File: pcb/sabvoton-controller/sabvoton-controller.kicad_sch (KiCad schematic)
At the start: 27 parts, among them J1 Conn_02x03_Counter_Clockwise, J2 Conn_01x30, U1 ESP32-WROOM-32, U2 XL7015E1, U3 XL7015E1

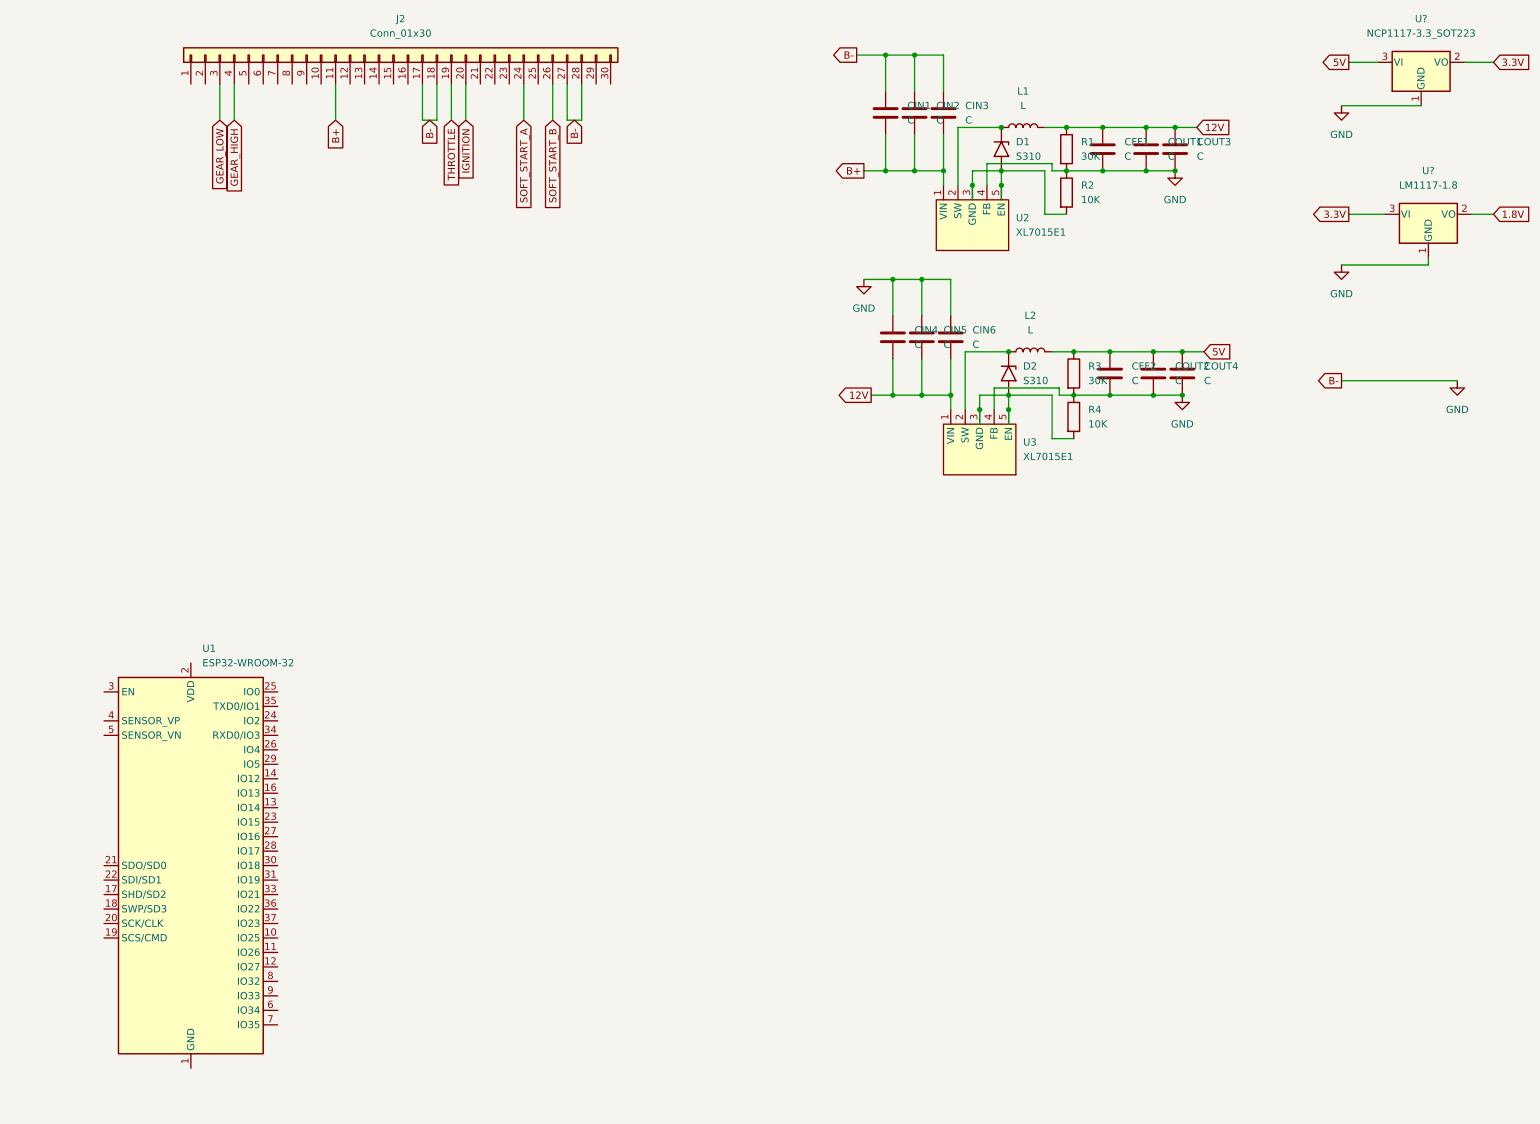
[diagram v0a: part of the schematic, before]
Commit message: Added power to the ESP32
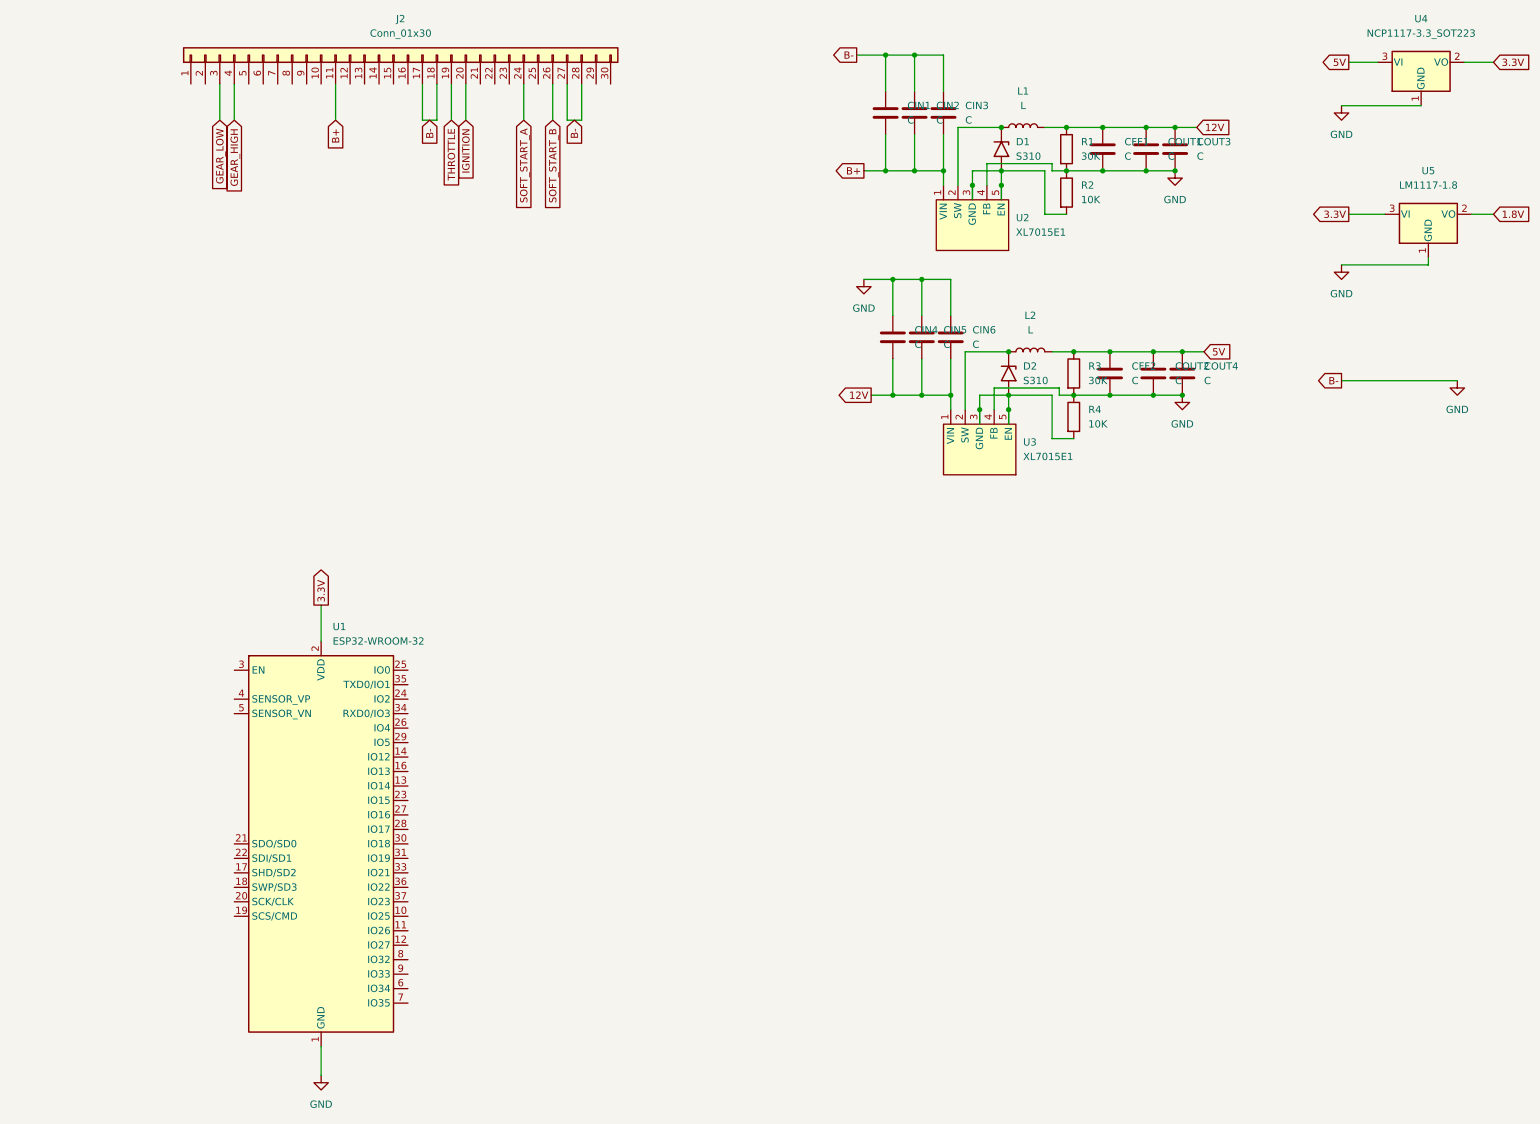
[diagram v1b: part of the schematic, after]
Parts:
- gave numbers to parts that had none: 2
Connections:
- net 3.3V: now also U1.2 (VDD)
- net GND: now also U1.1 (GND), U1.15 (GND), U1.38 (GND), U1.39 (GND)
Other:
- moved on the sheet: U1
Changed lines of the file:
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@@
+    (stroke (width 0) (type default) (color 0 0 0 0))
+  )
+  (wire (pts (xy 392.43 228.6) (xy 392.43 233.68))
     (stroke (width 0) (type default) (color 0 0 0 0))
   )
@@
     (stroke (width 0) (type default) (color 0 0 0 0))
   )
+  (wire (pts (xy 392.43 151.13) (xy 392.43 157.48))
+    (stroke (width 0) (type default) (color 0 0 0 0))
+  )
   (wire (pts (xy 571.5 63.5) (xy 585.47 63.5))
     (stroke (width 0) (type default) (color 0 0 0 0))
@@
   (wire (pts (xy 435.61 59.69) (xy 435.61 66.04))
     (stroke (width 0) (type default) (color 0 0 0 0))
+  )
+  (global_label "3.3V" (shape output) (at 392.43 151.13 90) (fields_autoplaced)
+    (effects (font (size 1.27 1.27)) (justify left))
+    (property "Intersheet References" "${INTERSHEET_REFS}" (id 0) (at 392.5094 144.6045 90)
+      (effects (font (size 1.27 1.27)) (justify left) hide)
+    )
   )
   (global_label "5V" (shape input) (at 547.37 106.68 0) (fields_autoplaced)
@@
   (symbol (lib_id "Regulator_Linear:LM1117-1.8") (at 586.74 82.55 0) (unit 1)
     (in_bom yes) (on_board yes) (fields_autoplaced)
-    (property "Reference" "U?" (id 0) (at 586.74 74.93 0))
+    (property "Reference" "U5" (id 0) (at 586.74 74.93 0))
     (property "Value" "LM1117-1.8" (id 1) (at 586.74 77.47 0))
     (property "Footprint" "Package_TO_SOT_SMD:SOT-223-3_TabPin2" (id 2) (at 586.74 82.55 0)
@@
     (pin "2")
   )
+  (symbol (lib_id "power:GND") (at 392.43 233.68 0) (unit 1)
+    (in_bom yes) (on_board yes) (fields_autoplaced)
+    (property "Reference" "#PWR0101" (id 0) (at 392.43 240.03 0)
+      (effects (font (size 1.27 1.27)) hide)
+    )
+    (property "Value" "GND" (id 1) (at 392.43 238.76 0))
+    (property "Footprint" "" (id 2) (at 392.43 233.68 0)
+      (effects (font (size 1.27 1.27)) hide)
+    )
+    (property "Datasheet" "" (id 3) (at 392.43 233.68 0)
+      (effects (font (size 1.27 1.27)) hide)
+    )
+    (pin "1")
+  )
   (symbol (lib_id "Diode:1.5KExxA") (at 511.81 71.12 270) (unit 1)
     (in_bom yes) (on_board yes) (fields_autoplaced)
@@
   (symbol (lib_id "power:GND") (at 571.5 63.5 0) (unit 1)
     (in_bom yes) (on_board yes) (fields_autoplaced)
-    (property "Reference" "#PWR?" (id 0) (at 571.5 69.85 0)
+    (property "Reference" "#PWR0102" (id 0) (at 571.5 69.85 0)
       (effects (font (size 1.27 1.27)) hide)
     )
@@
   (symbol (lib_id "power:GND") (at 591.82 111.76 0) (unit 1)
     (in_bom yes) (on_board yes) (fields_autoplaced)
-    (property "Reference" "#PWR?" (id 0) (at 591.82 118.11 0)
+    (property "Reference" "#PWR0103" (id 0) (at 591.82 118.11 0)
       (effects (font (size 1.27 1.27)) hide)
     )
@@
   (symbol (lib_id "Regulator_Linear:NCP1117-3.3_SOT223") (at 585.47 55.88 0) (unit 1)
     (in_bom yes) (on_board yes) (fields_autoplaced)
-    (property "Reference" "U?" (id 0) (at 585.47 48.26 0))
+    (property "Reference" "U4" (id 0) (at 585.47 48.26 0))
     (property "Value" "NCP1117-3.3_SOT223" (id 1) (at 585.47 50.8 0))
     (property "Footprint" "Package_TO_SOT_SMD:SOT-223-3_TabPin2" (id 2) (at 585.47 50.8 0)
@@
     (pin "2")
   )
-  (symbol (lib_id "RF_Module:ESP32-WROOM-32") (at 369.57 196.85 0) (unit 1)
-    (in_bom yes) (on_board yes) (fields_autoplaced)
-    (property "Reference" "U1" (id 0) (at 371.5894 158.75 0)
-      (effects (font (size 1.27 1.27)) (justify left))
-    )
-    (property "Value" "ESP32-WROOM-32" (id 1) (at 371.5894 161.29 0)
-      (effects (font (size 1.27 1.27)) (justify left))
-    )
-    (property "Footprint" "RF_Module:ESP32-WROOM-32" (id 2) (at 369.57 234.95 0)
-      (effects (font (size 1.27 1.27)) hide)
-    )
-    (property "Datasheet" "https://www.espressif.com/sites/default/files/documentation/esp32-wroom-32_datasheet_en.pdf" (id 3) (at 361.95 195.58 0)
+  (symbol (lib_id "RF_Module:ESP32-WROOM-32") (at 392.43 193.04 0) (unit 1)
+    (in_bom yes) (on_board yes) (fields_autoplaced)
+    (property "Reference" "U1" (id 0) (at 394.4494 154.94 0)
+      (effects (font (size 1.27 1.27)) (justify left))
+    )
+    (property "Value" "ESP32-WROOM-32" (id 1) (at 394.4494 157.48 0)
+      (effects (font (size 1.27 1.27)) (justify left))
+    )
+    (property "Footprint" "RF_Module:ESP32-WROOM-32" (id 2) (at 392.43 231.14 0)
+      (effects (font (size 1.27 1.27)) hide)
+    )
+    (property "Datasheet" "https://www.espressif.com/sites/default/files/documentation/esp32-wroom-32_datasheet_en.pdf" (id 3) (at 384.81 191.77 0)
       (effects (font (size 1.27 1.27)) hide)
     )
@@
   (symbol (lib_id "power:GND") (at 571.5 91.44 0) (unit 1)
     (in_bom yes) (on_board yes) (fields_autoplaced)
-    (property "Reference" "#PWR?" (id 0) (at 571.5 97.79 0)
+    (property "Reference" "#PWR0104" (id 0) (at 571.5 97.79 0)
       (effects (font (size 1.27 1.27)) hide)
     )
@@
       (reference "#PWR03") (unit 1) (value "GND") (footprint "")
     )
+    (path "/503c752c-7842-4267-a639-6f3d9aa0fe2a"
+      (reference "#PWR0101") (unit 1) (value "GND") (footprint "")
+    )
     (path "/5282e63d-cfea-46aa-b976-c6a9cdec0d63"
-      (reference "#PWR?") (unit 1) (value "GND") (footprint "")
+      (reference "#PWR0102") (unit 1) (value "GND") (footprint "")
     )
     (path "/972aac5e-c9a1-4c35-9267-e07a8dc2778e"
-      (reference "#PWR?") (unit 1) (value "GND") (footprint "")
+      (reference "#PWR0103") (unit 1) (value "GND") (footprint "")
     )
     (path "/e7b8caad-8c25-46ee-a171-3c952ff2378f"
-      (reference "#PWR?") (unit 1) (value "GND") (footprint "")
+      (reference "#PWR0104") (unit 1) (value "GND") (footprint "")
     )
     (path "/d492c89a-b073-4f16-8a2d-e57b90ec8edc"
@@
       (reference "U3") (unit 1) (value "XL7015E1") (footprint "Package_TO_SOT_SMD:TO-252-5_TabPin3")
     )
+    (path "/9a47097d-06a5-4183-845e-85572096854c"
+      (reference "U4") (unit 1) (value "NCP1117-3.3_SOT223") (footprint "Package_TO_SOT_SMD:SOT-223-3_TabPin2")
+    )
     (path "/4029d2d4-cecc-41e8-82bd-e371ea31d069"
-      (reference "U?") (unit 1) (value "LM1117-1.8") (footprint "Package_TO_SOT_SMD:SOT-223-3_TabPin2")
-    )
-    (path "/9a47097d-06a5-4183-845e-85572096854c"
-      (reference "U?") (unit 1) (value "NCP1117-3.3_SOT223") (footprint "Package_TO_SOT_SMD:SOT-223-3_TabPin2")
-    )
-  )
+      (reference "U5") (unit 1) (value "LM1117-1.8") (footprint "Package_TO_SOT_SMD:SOT-223-3_TabPin2")
+    )
+  )

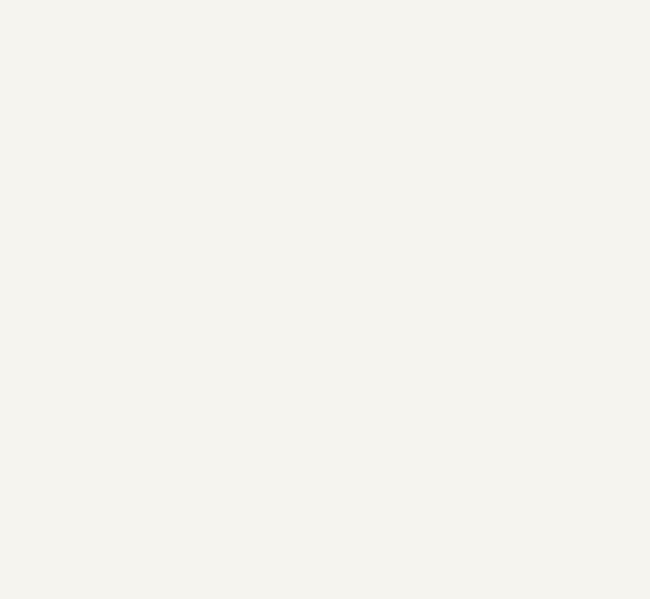
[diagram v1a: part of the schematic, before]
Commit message: Added power switch circuit
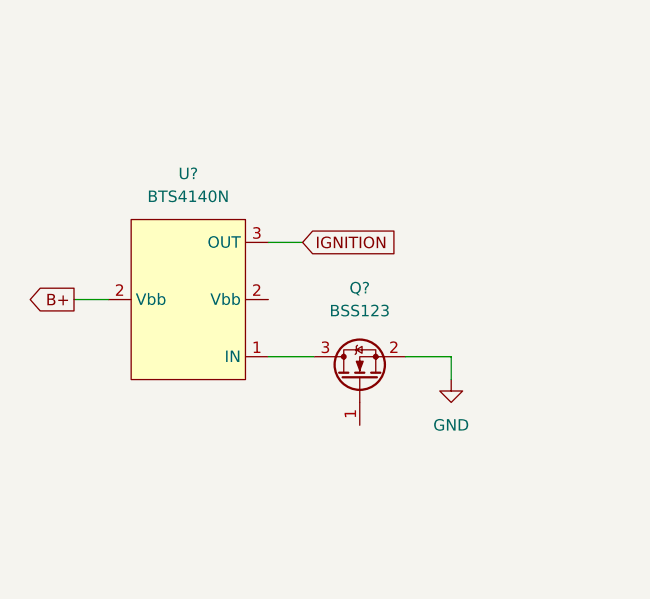
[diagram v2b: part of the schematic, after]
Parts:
- added Q?: BSS123, Package_TO_SOT_SMD:SOT-23, symbol Transistor_FET:BSS123
- added U?: BTS4140N, Package_TO_SOT_SMD:SOT-223-3_TabPin2, symbol KT_Display:BTS4140N
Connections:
- net B+: now also U?.2 (Vbb)
- net GND: now also Q?.2 (S)
- net IGNITION: now also U?.3 (OUT)
- new net: Q?.3 (D), U?.1 (IN)
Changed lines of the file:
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@@
+    (stroke (width 0) (type default) (color 0 0 0 0))
+  )
+  (wire (pts (xy 248.92 88.9) (xy 254 88.9))
     (stroke (width 0) (type default) (color 0 0 0 0))
   )
@@
     (stroke (width 0) (type default) (color 0 0 0 0))
   )
+  (wire (pts (xy 269.24 88.9) (xy 269.24 91.44))
+    (stroke (width 0) (type default) (color 0 0 0 0))
+  )
   (wire (pts (xy 427.99 59.69) (xy 427.99 66.04))
     (stroke (width 0) (type default) (color 0 0 0 0))
@@
     (stroke (width 0) (type default) (color 0 0 0 0))
   )
+  (wire (pts (xy 227.33 82.55) (xy 231.14 82.55))
+    (stroke (width 0) (type default) (color 0 0 0 0))
+  )
   (wire (pts (xy 487.68 74.93) (xy 491.49 74.93))
     (stroke (width 0) (type default) (color 0 0 0 0))
@@
     (stroke (width 0) (type default) (color 0 0 0 0))
   )
+  (wire (pts (xy 264.16 88.9) (xy 269.24 88.9))
+    (stroke (width 0) (type default) (color 0 0 0 0))
+  )
   (wire (pts (xy 496.57 54.61) (xy 496.57 60.96))
     (stroke (width 0) (type default) (color 0 0 0 0))
@@
   )
   (wire (pts (xy 496.57 68.58) (xy 496.57 74.93))
+    (stroke (width 0) (type default) (color 0 0 0 0))
+  )
+  (wire (pts (xy 248.92 76.2) (xy 252.73 76.2))
     (stroke (width 0) (type default) (color 0 0 0 0))
   )
@@
     )
   )
+  (global_label "B+" (shape output) (at 227.33 82.55 180) (fields_autoplaced)
+    (effects (font (size 1.27 1.27)) (justify right))
+    (property "Intersheet References" "${INTERSHEET_REFS}" (id 0) (at 222.0745 82.4706 0)
+      (effects (font (size 1.27 1.27)) (justify right) hide)
+    )
+  )
   (global_label "12V" (shape input) (at 546.1 67.31 0) (fields_autoplaced)
     (effects (font (size 1.27 1.27)) (justify left))
@@
     )
   )
+  (global_label "IGNITION" (shape input) (at 252.73 76.2 0) (fields_autoplaced)
+    (effects (font (size 1.27 1.27)) (justify left))
+    (property "Intersheet References" "${INTERSHEET_REFS}" (id 0) (at 263.1864 76.2794 0)
+      (effects (font (size 1.27 1.27)) (justify left) hide)
+    )
+  )
   (symbol (lib_id "power:GND") (at 487.68 93.98 0) (unit 1)
     (in_bom yes) (on_board yes) (fields_autoplaced)
@@
     (pin "2")
   )
+  (symbol (lib_id "KT_Display:BTS4140N") (at 241.3 82.55 90) (unit 1)
+    (in_bom yes) (on_board yes) (fields_autoplaced)
+    (property "Reference" "U?" (id 0) (at 240.03 68.58 90))
+    (property "Value" "BTS4140N" (id 1) (at 240.03 71.12 90))
+    (property "Footprint" "Package_TO_SOT_SMD:SOT-223-3_TabPin2" (id 2) (at 241.3 82.55 0)
+      (effects (font (size 1.27 1.27)) hide)
+    )
+    (property "Datasheet" "" (id 3) (at 241.3 82.55 0)
+      (effects (font (size 1.27 1.27)) hide)
+    )
+    (pin "1")
+    (pin "2")
+    (pin "2")
+    (pin "3")
+  )
   (symbol (lib_id "Device:C") (at 543.56 110.49 0) (unit 1)
     (in_bom yes) (on_board yes) (fields_autoplaced)
@@
     (pin "1")
     (pin "2")
+  )
+  (symbol (lib_id "Transistor_FET:BSS123") (at 259.08 91.44 90) (unit 1)
+    (in_bom yes) (on_board yes) (fields_autoplaced)
+    (property "Reference" "Q?" (id 0) (at 259.08 81.28 90))
+    (property "Value" "BSS123" (id 1) (at 259.08 83.82 90))
+    (property "Footprint" "Package_TO_SOT_SMD:SOT-23" (id 2) (at 260.985 86.36 0)
+      (effects (font (size 1.27 1.27) italic) (justify left) hide)
+    )
+    (property "Datasheet" "http://www.diodes.com/assets/Datasheets/ds30366.pdf" (id 3) (at 259.08 91.44 0)
+      (effects (font (size 1.27 1.27)) (justify left) hide)
+    )
+    (pin "1")
+    (pin "2")
+    (pin "3")
   )
   (symbol (lib_id "Device:C") (at 542.29 71.12 0) (unit 1)
@@
     (pin "2")
   )
+  (symbol (lib_id "power:GND") (at 269.24 91.44 0) (unit 1)
+    (in_bom yes) (on_board yes) (fields_autoplaced)
+    (property "Reference" "#PWR?" (id 0) (at 269.24 97.79 0)
+      (effects (font (size 1.27 1.27)) hide)
+    )
+    (property "Value" "GND" (id 1) (at 269.24 96.52 0))
+    (property "Footprint" "" (id 2) (at 269.24 91.44 0)
+      (effects (font (size 1.27 1.27)) hide)
+    )
+    (property "Datasheet" "" (id 3) (at 269.24 91.44 0)
+      (effects (font (size 1.27 1.27)) hide)
+    )
+    (pin "1")
+  )
   (symbol (lib_id "Connector_Generic:Conn_01x30") (at 405.13 54.61 90) (unit 1)
     (in_bom yes) (on_board yes) (fields_autoplaced)
@@
       (reference "#PWR0104") (unit 1) (value "GND") (footprint "")
     )
+    (path "/d1a72cb7-756b-42ca-82a5-1e45fcb3112e"
+      (reference "#PWR?") (unit 1) (value "GND") (footprint "")
+    )
     (path "/d492c89a-b073-4f16-8a2d-e57b90ec8edc"
       (reference "CFF1") (unit 1) (value "C") (footprint "Capacitor_SMD:C_1206_3216Metric_Pad1.33x1.80mm_HandSolder")
@@
       (reference "L2") (unit 1) (value "L") (footprint "Inductor_SMD:L_7.3x7.3_H3.5")
     )
+    (path "/bb9abdb5-aafb-4170-b2f3-4f71fedeccf0"
+      (reference "Q?") (unit 1) (value "BSS123") (footprint "Package_TO_SOT_SMD:SOT-23")
+    )
     (path "/3c54a24c-10be-4236-a15f-1623c52b157c"
       (reference "R1") (unit 1) (value "30K") (footprint "Resistor_SMD:R_1206_3216Metric_Pad1.30x1.75mm_HandSolder")
@@
       (reference "U5") (unit 1) (value "LM1117-1.8") (footprint "Package_TO_SOT_SMD:SOT-223-3_TabPin2")
     )
-  )
+    (path "/66ed68f5-4670-4078-9b15-61561f4028b6"
+      (reference "U?") (unit 1) (value "BTS4140N") (footprint "Package_TO_SOT_SMD:SOT-223-3_TabPin2")
+    )
+  )
